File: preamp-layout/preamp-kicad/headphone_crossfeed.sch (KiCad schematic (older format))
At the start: 18 parts, among them J78 Conn_01x04_Female, J79 Conn_01x04_Male, SW12 SW_DPDT_x2

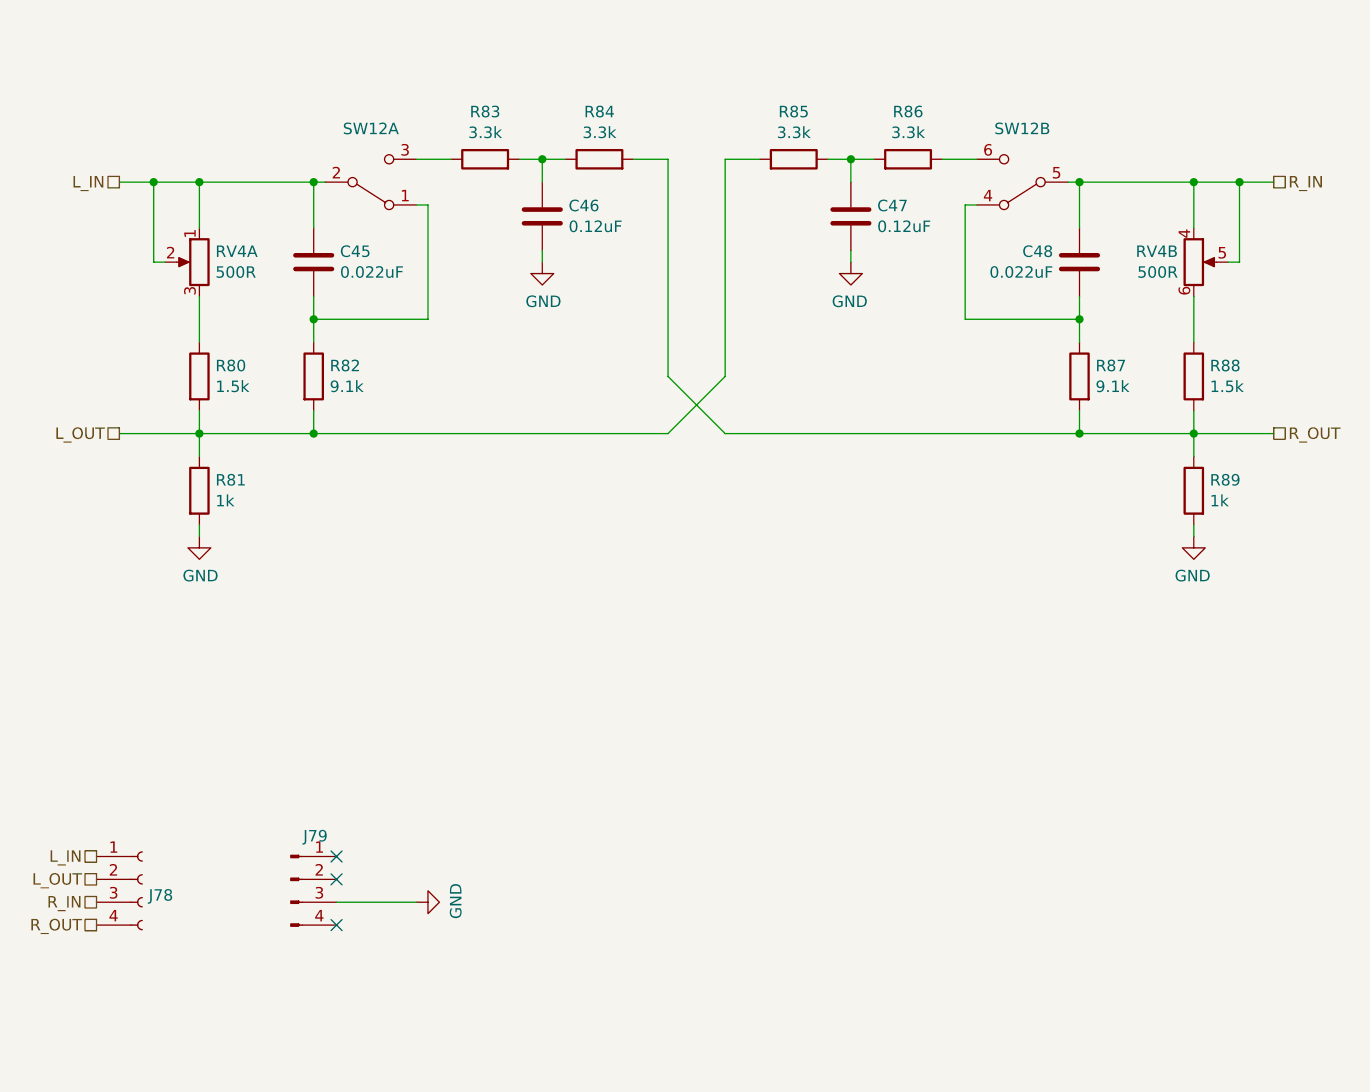
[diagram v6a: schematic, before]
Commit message: RefDes Update
Re-ran refdes assignment, updated BOM accordingly.
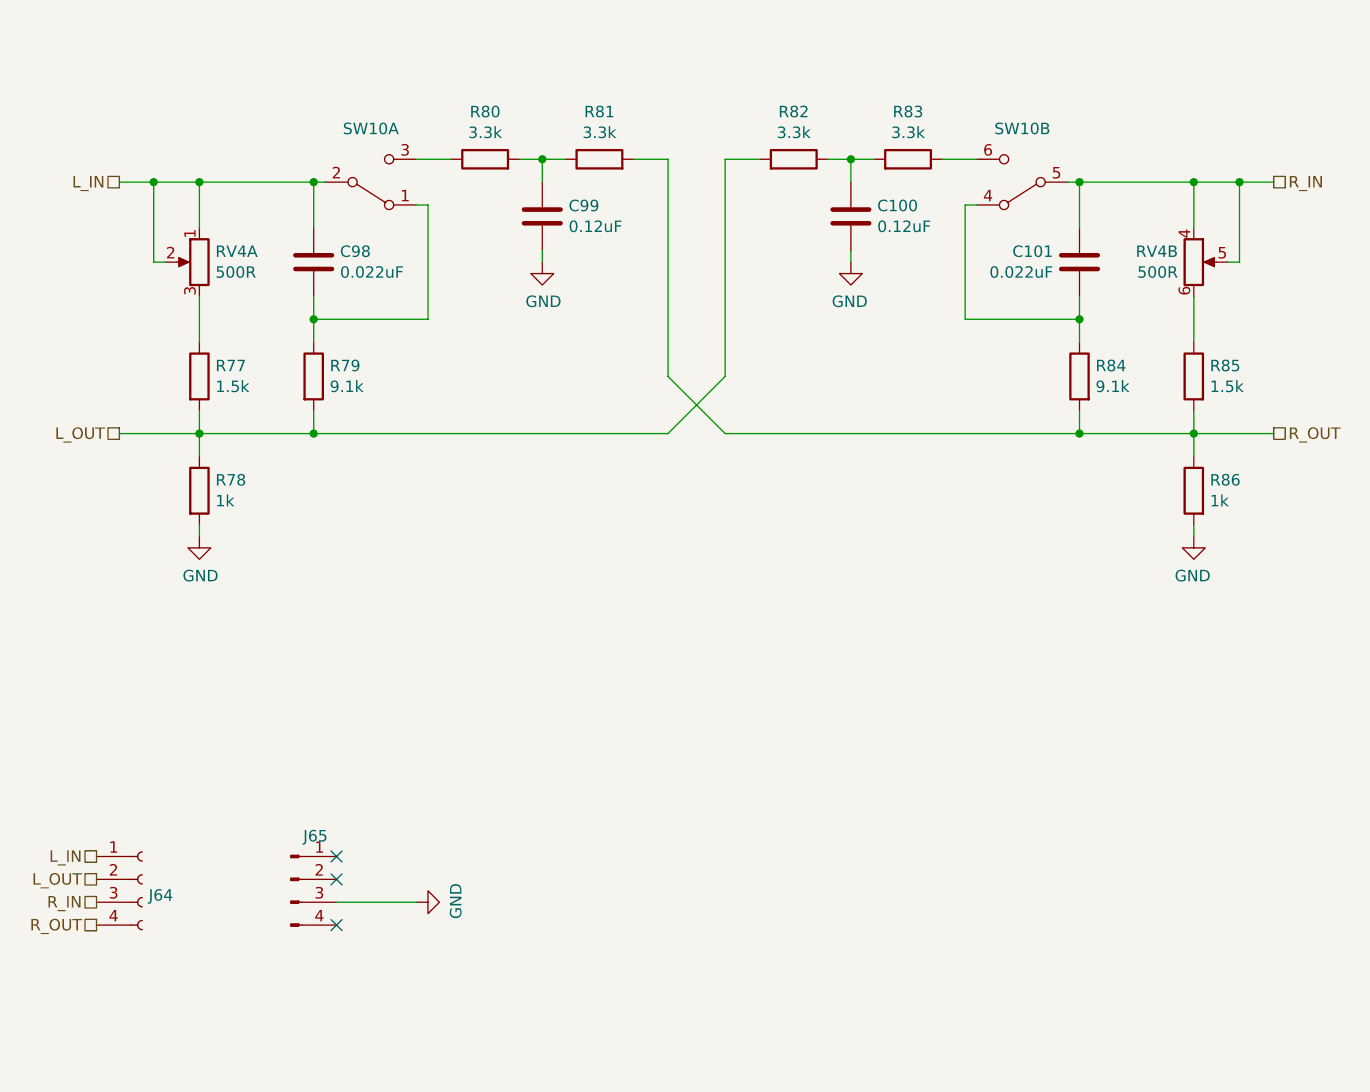
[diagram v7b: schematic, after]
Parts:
- renumbered C47 to C100, C48 to C101, C45 to C98, C46 to C99, J78 to J64, J79 to J65, R80 to R77, R81 to R78, R82 to R79, R83 to R80, R84 to R81, R85 to R82, R86 to R83, R87 to R84, R88 to R85, R89 to R86, SW12 to SW10
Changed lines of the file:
@@
 P 3850 4150
 AR Path="/5E4A803E/5EE90D95" Ref="R?"  Part="1"
-AR Path="/5E4A803E/5EE80145/5EE90D95" Ref="R81"  Part="1"
-F 0 "R81" H 3920 4196 50  0000 L CNN
+AR Path="/5E4A803E/5EE80145/5EE90D95" Ref="R78"  Part="1"
+F 0 "R78" H 3920 4196 50  0000 L CNN
 F 1 "1k" H 3920 4105 50  0000 L CNN
 F 2 "Resistor_SMD:R_1206_3216Metric_Pad1.42x1.75mm_HandSolder" V 3780 4150 50  0001 C CNN
@@
 P 4350 3650
 AR Path="/5E4A803E/5EE90D9B" Ref="R?"  Part="1"
-AR Path="/5E4A803E/5EE80145/5EE90D9B" Ref="R82"  Part="1"
-F 0 "R82" H 4420 3696 50  0000 L CNN
+AR Path="/5E4A803E/5EE80145/5EE90D9B" Ref="R79"  Part="1"
+F 0 "R79" H 4420 3696 50  0000 L CNN
 F 1 "9.1k" H 4420 3605 50  0000 L CNN
 F 2 "Resistor_SMD:R_1206_3216Metric_Pad1.42x1.75mm_HandSolder" V 4280 3650 50  0001 C CNN
@@
 P 5100 2700
 AR Path="/5E4A803E/5EE90DA1" Ref="R?"  Part="1"
-AR Path="/5E4A803E/5EE80145/5EE90DA1" Ref="R83"  Part="1"
-F 0 "R83" V 5307 2700 50  0000 C CNN
+AR Path="/5E4A803E/5EE80145/5EE90DA1" Ref="R80"  Part="1"
+F 0 "R80" V 5307 2700 50  0000 C CNN
 F 1 "3.3k" V 5216 2700 50  0000 C CNN
 F 2 "Resistor_SMD:R_1206_3216Metric_Pad1.42x1.75mm_HandSolder" V 5030 2700 50  0001 C CNN
@@
 P 4350 3150
 AR Path="/5E4A803E/5EE90DA7" Ref="C?"  Part="1"
-AR Path="/5E4A803E/5EE80145/5EE90DA7" Ref="C45"  Part="1"
-F 0 "C45" H 4465 3196 50  0000 L CNN
+AR Path="/5E4A803E/5EE80145/5EE90DA7" Ref="C98"  Part="1"
+F 0 "C98" H 4465 3196 50  0000 L CNN
 F 1 "0.022uF" H 4465 3105 50  0000 L CNN
 F 2 "Capacitor_SMD:C_0805_2012Metric_Pad1.15x1.40mm_HandSolder" H 4388 3000 50  0001 C CNN
@@
 P 5350 2950
 AR Path="/5E4A803E/5EE90DAD" Ref="C?"  Part="1"
-AR Path="/5E4A803E/5EE80145/5EE90DAD" Ref="C46"  Part="1"
-F 0 "C46" H 5465 2996 50  0000 L CNN
+AR Path="/5E4A803E/5EE80145/5EE90DAD" Ref="C99"  Part="1"
+F 0 "C99" H 5465 2996 50  0000 L CNN
 F 1 "0.12uF" H 5465 2905 50  0000 L CNN
 F 2 "Capacitor_SMD:C_0805_2012Metric_Pad1.15x1.40mm_HandSolder" H 5388 2800 50  0001 C CNN
@@
 P 5600 2700
 AR Path="/5E4A803E/5EE90DB3" Ref="R?"  Part="1"
-AR Path="/5E4A803E/5EE80145/5EE90DB3" Ref="R84"  Part="1"
-F 0 "R84" V 5807 2700 50  0000 C CNN
+AR Path="/5E4A803E/5EE80145/5EE90DB3" Ref="R81"  Part="1"
+F 0 "R81" V 5807 2700 50  0000 C CNN
 F 1 "3.3k" V 5716 2700 50  0000 C CNN
 F 2 "Resistor_SMD:R_1206_3216Metric_Pad1.42x1.75mm_HandSolder" V 5530 2700 50  0001 C CNN
@@
 P 4600 2800
 AR Path="/5E4A803E/5EE90DB9" Ref="SW?"  Part="1"
-AR Path="/5E4A803E/5EE80145/5EE90DB9" Ref="SW12"  Part="1"
-F 0 "SW12" H 4600 2567 50  0000 C CNN
+AR Path="/5E4A803E/5EE80145/5EE90DB9" Ref="SW10"  Part="1"
+F 0 "SW10" H 4600 2567 50  0000 C CNN
 F 1 "SW_DPDT_x2" V 4645 2612 50  0001 R CNN
 F 2 "" H 4600 2800 50  0001 C CNN
@@
 P 7450 2800
 AR Path="/5E4A803E/5EE90DBF" Ref="SW?"  Part="2"
-AR Path="/5E4A803E/5EE80145/5EE90DBF" Ref="SW12"  Part="2"
-F 0 "SW12" H 7450 2567 50  0000 C CNN
+AR Path="/5E4A803E/5EE80145/5EE90DBF" Ref="SW10"  Part="2"
+F 0 "SW10" H 7450 2567 50  0000 C CNN
 F 1 "SW_DPDT_x2" V 7495 2613 50  0001 R CNN
 F 2 "" H 7450 2800 50  0001 C CNN
@@
 AR Path="/6009D432/5EE90DC5" Ref="#PWR?"  Part="1"
 AR Path="/5E4A803E/5EE90DC5" Ref="#PWR?"  Part="1"
-AR Path="/5E4A803E/5EE80145/5EE90DC5" Ref="#PWR0114"  Part="1"
-F 0 "#PWR0114" H 3850 4100 50  0001 C CNN
+AR Path="/5E4A803E/5EE80145/5EE90DC5" Ref="#PWR097"  Part="1"
+F 0 "#PWR097" H 3850 4100 50  0001 C CNN
 F 1 "GND" H 3855 4177 50  0000 C CNN
 F 2 "" H 3850 4350 50  0001 C CNN
@@
 AR Path="/6009D432/5EE90DD0" Ref="#PWR?"  Part="1"
 AR Path="/5E4A803E/5EE90DD0" Ref="#PWR?"  Part="1"
-AR Path="/5E4A803E/5EE80145/5EE90DD0" Ref="#PWR0116"  Part="1"
-F 0 "#PWR0116" H 5350 2900 50  0001 C CNN
+AR Path="/5E4A803E/5EE80145/5EE90DD0" Ref="#PWR099"  Part="1"
+F 0 "#PWR099" H 5350 2900 50  0001 C CNN
 F 1 "GND" H 5355 2977 50  0000 C CNN
 F 2 "" H 5350 3150 50  0001 C CNN
@@
 P 3850 3650
 AR Path="/5E4A803E/5EE90DD6" Ref="R?"  Part="1"
-AR Path="/5E4A803E/5EE80145/5EE90DD6" Ref="R80"  Part="1"
-F 0 "R80" H 3920 3696 50  0000 L CNN
+AR Path="/5E4A803E/5EE80145/5EE90DD6" Ref="R77"  Part="1"
+F 0 "R77" H 3920 3696 50  0000 L CNN
 F 1 "1.5k" H 3920 3605 50  0000 L CNN
 F 2 "Resistor_SMD:R_1206_3216Metric_Pad1.42x1.75mm_HandSolder" V 3780 3650 50  0001 C CNN
@@
 P 8200 4150
 AR Path="/5E4A803E/5EE90DF0" Ref="R?"  Part="1"
-AR Path="/5E4A803E/5EE80145/5EE90DF0" Ref="R89"  Part="1"
-F 0 "R89" H 8130 4196 50  0000 R CNN
+AR Path="/5E4A803E/5EE80145/5EE90DF0" Ref="R86"  Part="1"
+F 0 "R86" H 8130 4196 50  0000 R CNN
 F 1 "1k" H 8130 4105 50  0000 R CNN
 F 2 "Resistor_SMD:R_1206_3216Metric_Pad1.42x1.75mm_HandSolder" V 8130 4150 50  0001 C CNN
@@
 P 7700 3650
 AR Path="/5E4A803E/5EE90DF6" Ref="R?"  Part="1"
-AR Path="/5E4A803E/5EE80145/5EE90DF6" Ref="R87"  Part="1"
-F 0 "R87" H 7630 3696 50  0000 R CNN
+AR Path="/5E4A803E/5EE80145/5EE90DF6" Ref="R84"  Part="1"
+F 0 "R84" H 7630 3696 50  0000 R CNN
 F 1 "9.1k" H 7630 3605 50  0000 R CNN
 F 2 "Resistor_SMD:R_1206_3216Metric_Pad1.42x1.75mm_HandSolder" V 7630 3650 50  0001 C CNN
@@
 P 6950 2700
 AR Path="/5E4A803E/5EE90DFC" Ref="R?"  Part="1"
-AR Path="/5E4A803E/5EE80145/5EE90DFC" Ref="R86"  Part="1"
-F 0 "R86" V 7157 2700 50  0000 C CNN
+AR Path="/5E4A803E/5EE80145/5EE90DFC" Ref="R83"  Part="1"
+F 0 "R83" V 7157 2700 50  0000 C CNN
 F 1 "3.3k" V 7066 2700 50  0000 C CNN
 F 2 "Resistor_SMD:R_1206_3216Metric_Pad1.42x1.75mm_HandSolder" V 6880 2700 50  0001 C CNN
@@
 P 7700 3150
 AR Path="/5E4A803E/5EE90E02" Ref="C?"  Part="1"
-AR Path="/5E4A803E/5EE80145/5EE90E02" Ref="C48"  Part="1"
-F 0 "C48" H 7815 3196 50  0000 L CNN
+AR Path="/5E4A803E/5EE80145/5EE90E02" Ref="C101"  Part="1"
+F 0 "C101" H 7815 3196 50  0000 L CNN
 F 1 "0.022uF" H 7815 3105 50  0000 L CNN
 F 2 "Capacitor_SMD:C_0805_2012Metric_Pad1.15x1.40mm_HandSolder" H 7738 3000 50  0001 C CNN
@@
 P 6700 2950
 AR Path="/5E4A803E/5EE90E08" Ref="C?"  Part="1"
-AR Path="/5E4A803E/5EE80145/5EE90E08" Ref="C47"  Part="1"
-F 0 "C47" H 6585 2996 50  0000 R CNN
+AR Path="/5E4A803E/5EE80145/5EE90E08" Ref="C100"  Part="1"
+F 0 "C100" H 6585 2996 50  0000 R CNN
 F 1 "0.12uF" H 6585 2905 50  0000 R CNN
 F 2 "Capacitor_SMD:C_0805_2012Metric_Pad1.15x1.40mm_HandSolder" H 6738 2800 50  0001 C CNN
@@
 P 6450 2700
 AR Path="/5E4A803E/5EE90E0E" Ref="R?"  Part="1"
-AR Path="/5E4A803E/5EE80145/5EE90E0E" Ref="R85"  Part="1"
-F 0 "R85" V 6657 2700 50  0000 C CNN
+AR Path="/5E4A803E/5EE80145/5EE90E0E" Ref="R82"  Part="1"
+F 0 "R82" V 6657 2700 50  0000 C CNN
 F 1 "3.3k" V 6566 2700 50  0000 C CNN
 F 2 "Resistor_SMD:R_1206_3216Metric_Pad1.42x1.75mm_HandSolder" V 6380 2700 50  0001 C CNN
@@
 AR Path="/6009D432/5EE90E14" Ref="#PWR?"  Part="1"
 AR Path="/5E4A803E/5EE90E14" Ref="#PWR?"  Part="1"
-AR Path="/5E4A803E/5EE80145/5EE90E14" Ref="#PWR0118"  Part="1"
-F 0 "#PWR0118" H 8200 4100 50  0001 C CNN
+AR Path="/5E4A803E/5EE80145/5EE90E14" Ref="#PWR0101"  Part="1"
+F 0 "#PWR0101" H 8200 4100 50  0001 C CNN
 F 1 "GND" H 8205 4177 50  0000 C CNN
 F 2 "" H 8200 4350 50  0001 C CNN
@@
 AR Path="/6009D432/5EE90E1F" Ref="#PWR?"  Part="1"
 AR Path="/5E4A803E/5EE90E1F" Ref="#PWR?"  Part="1"
-AR Path="/5E4A803E/5EE80145/5EE90E1F" Ref="#PWR0117"  Part="1"
-F 0 "#PWR0117" H 6700 2900 50  0001 C CNN
+AR Path="/5E4A803E/5EE80145/5EE90E1F" Ref="#PWR0100"  Part="1"
+F 0 "#PWR0100" H 6700 2900 50  0001 C CNN
 F 1 "GND" H 6705 2977 50  0000 C CNN
 F 2 "" H 6700 3150 50  0001 C CNN
@@
 P 8200 3650
 AR Path="/5E4A803E/5EE90E25" Ref="R?"  Part="1"
-AR Path="/5E4A803E/5EE80145/5EE90E25" Ref="R88"  Part="1"
-F 0 "R88" H 8130 3696 50  0000 R CNN
+AR Path="/5E4A803E/5EE80145/5EE90E25" Ref="R85"  Part="1"
+F 0 "R85" H 8130 3696 50  0000 R CNN
 F 1 "1.5k" H 8130 3605 50  0000 R CNN
 F 2 "Resistor_SMD:R_1206_3216Metric_Pad1.42x1.75mm_HandSolder" V 8130 3650 50  0001 C CNN
@@
 L_IN
 $Comp
-L Connector:Conn_01x04_Female J78
+L Connector:Conn_01x04_Female J64
 U 1 1 5E7CDD58
 P 3600 5850
-F 0 "J78" H 3628 5780 50  0000 L CNN
+F 0 "J64" H 3628 5780 50  0000 L CNN
 F 1 "Conn_01x04_Female" H 3628 5735 50  0001 L CNN
 F 2 "Connector_PinHeader_2.54mm:PinHeader_1x04_P2.54mm_Vertical" H 3600 5850 50  0001 C CNN
@@
 NoConn ~ 4450 6050
 $Comp
-L Connector:Conn_01x04_Male J79
+L Connector:Conn_01x04_Male J65
 U 1 1 5EF52177
 P 4250 5850
-F 0 "J79" H 4358 6039 50  0000 C CNN
+F 0 "J65" H 4358 6039 50  0000 C CNN
 F 1 "Conn_01x04_Male" H 4358 6040 50  0001 C CNN
 F 2 "Connector_PinHeader_2.54mm:PinHeader_1x04_P2.54mm_Vertical" H 4250 5850 50  0001 C CNN
@@
 AR Path="/6009D432/5E7DF118" Ref="#PWR?"  Part="1"
 AR Path="/5E4A803E/5E7DF118" Ref="#PWR?"  Part="1"
-AR Path="/5E4A803E/5EE80145/5E7DF118" Ref="#PWR0115"  Part="1"
-F 0 "#PWR0115" H 4800 5700 50  0001 C CNN
+AR Path="/5E4A803E/5EE80145/5E7DF118" Ref="#PWR098"  Part="1"
+F 0 "#PWR098" H 4800 5700 50  0001 C CNN
 F 1 "GND" H 4805 5777 50  0000 C CNN
 F 2 "" H 4800 5950 50  0001 C CNN

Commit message: Prelim PCB layout
Work done to lay out PCBs. Saving in anticipation of creating branch with a different input switching topology.
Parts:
- RV4, SW10: footprint (none) -> Connector_PinHeader_2.54mm:PinHeader_1x03_P2.54mm_Vertical
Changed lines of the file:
@@
 F 0 "RV4" H 3780 3196 50  0000 R CNN
 F 1 "500R" H 3780 3105 50  0000 R CNN
-F 2 "" H 3850 3150 50  0001 C CNN
+F 2 "Connector_PinHeader_2.54mm:PinHeader_1x03_P2.54mm_Vertical" H 3850 3150 50  0001 C CNN
 F 3 "~" H 3850 3150 50  0001 C CNN
 	1    3850 3150
@@
 F 0 "RV4" H 8131 3196 50  0000 R CNN
 F 1 "500R" H 8131 3105 50  0000 R CNN
-F 2 "" H 8200 3150 50  0001 C CNN
+F 2 "Connector_PinHeader_2.54mm:PinHeader_1x03_P2.54mm_Vertical" H 8200 3150 50  0001 C CNN
 F 3 "~" H 8200 3150 50  0001 C CNN
 	2    8200 3150
@@
 F 0 "SW10" H 4600 2567 50  0000 C CNN
 F 1 "SW_DPDT_x2" V 4645 2612 50  0001 R CNN
-F 2 "" H 4600 2800 50  0001 C CNN
+F 2 "Connector_PinHeader_2.54mm:PinHeader_1x03_P2.54mm_Vertical" H 4600 2800 50  0001 C CNN
 F 3 "~" H 4600 2800 50  0001 C CNN
 	1    4600 2800
@@
 F 0 "SW10" H 7450 2567 50  0000 C CNN
 F 1 "SW_DPDT_x2" V 7495 2613 50  0001 R CNN
-F 2 "" H 7450 2800 50  0001 C CNN
+F 2 "Connector_PinHeader_2.54mm:PinHeader_1x03_P2.54mm_Vertical" H 7450 2800 50  0001 C CNN
 F 3 "~" H 7450 2800 50  0001 C CNN
 	2    7450 2800
